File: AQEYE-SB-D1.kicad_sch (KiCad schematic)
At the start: 72 parts, among them J1 GPIO15, J10 ZH06_PicoBlade, J11 DHT20, J12 AGS02MA, J13 +3.3V, J14 MB_PINS, J15 MB_CONNECTOR, J16 GND, J17 USB_D+, J18 USB_D-, J19 +5V, J2 DHT20_PAD, J20 GND, J21 SGP40-D-R4_CONN, J22 SCD40-D-R2_CONN, J23 STEMMA-QT, J24 WS_TVOC, J3 AGS02MA_PAD, J4 GPIO18, J5 ESP_RXD0, J6 ESP_TXD0, J7 I2C_SDA, J8 I2C_SCL, J9 ZH06_Pin, U1 SCD40-D-R2, U2 SGP40-D-R4, U3 AP22804AW5, U4 AP22804AW5

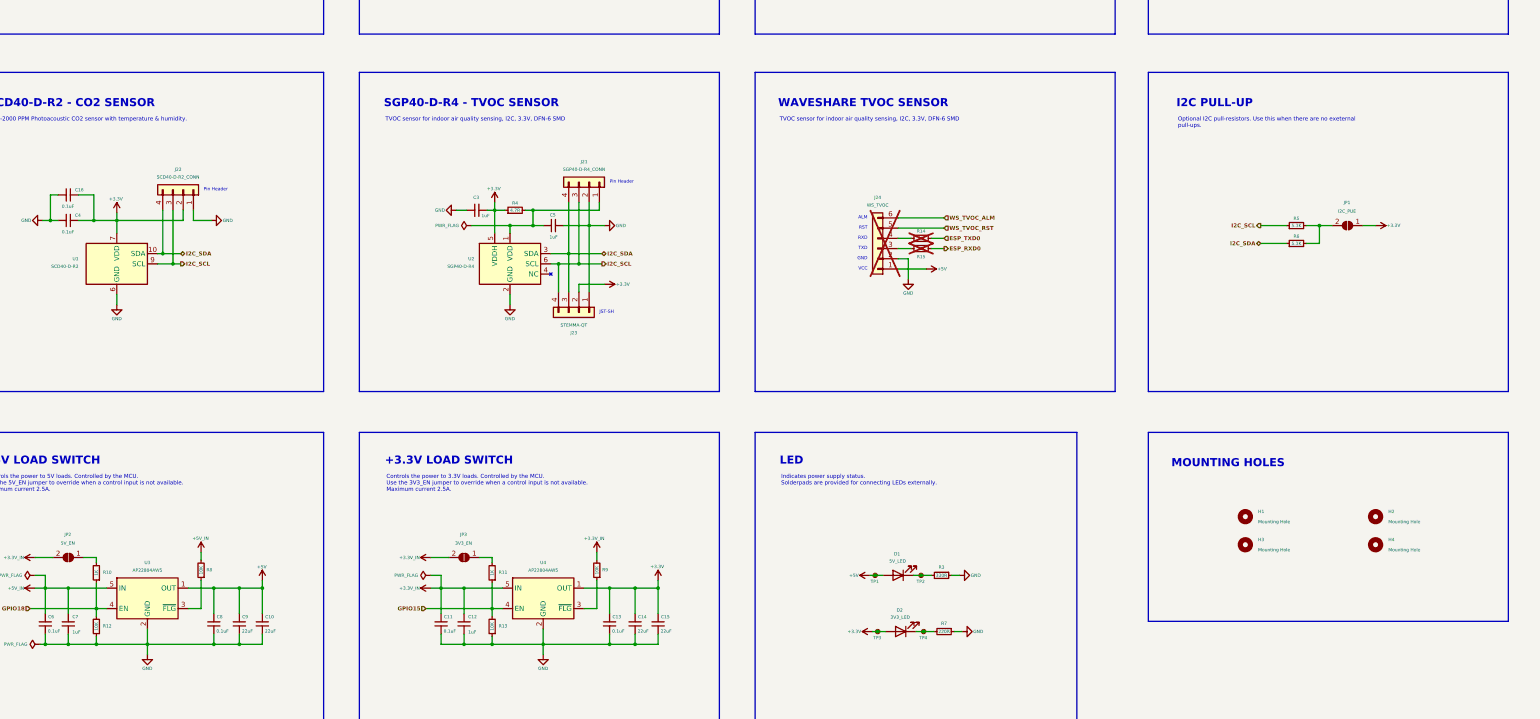
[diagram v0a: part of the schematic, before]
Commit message: Generated manufacturing files
- Schematic
  - Updated BoM.
  - Assigned all MPNs.
  - Added `Group by MPN-DNP` preset.
- PCB
  - Imported all changes to the PCB.
  - Cleaned up the Fab layers.
  - Added CIRCUITSTATE logo and GitHub link to schematic.
  - Applied teardrops.
  - Added board stackup table and characteristics.
  - DRC passes.
- Added KiExport configuration.
- Added Git scripts.
- Generated manufacturing files.
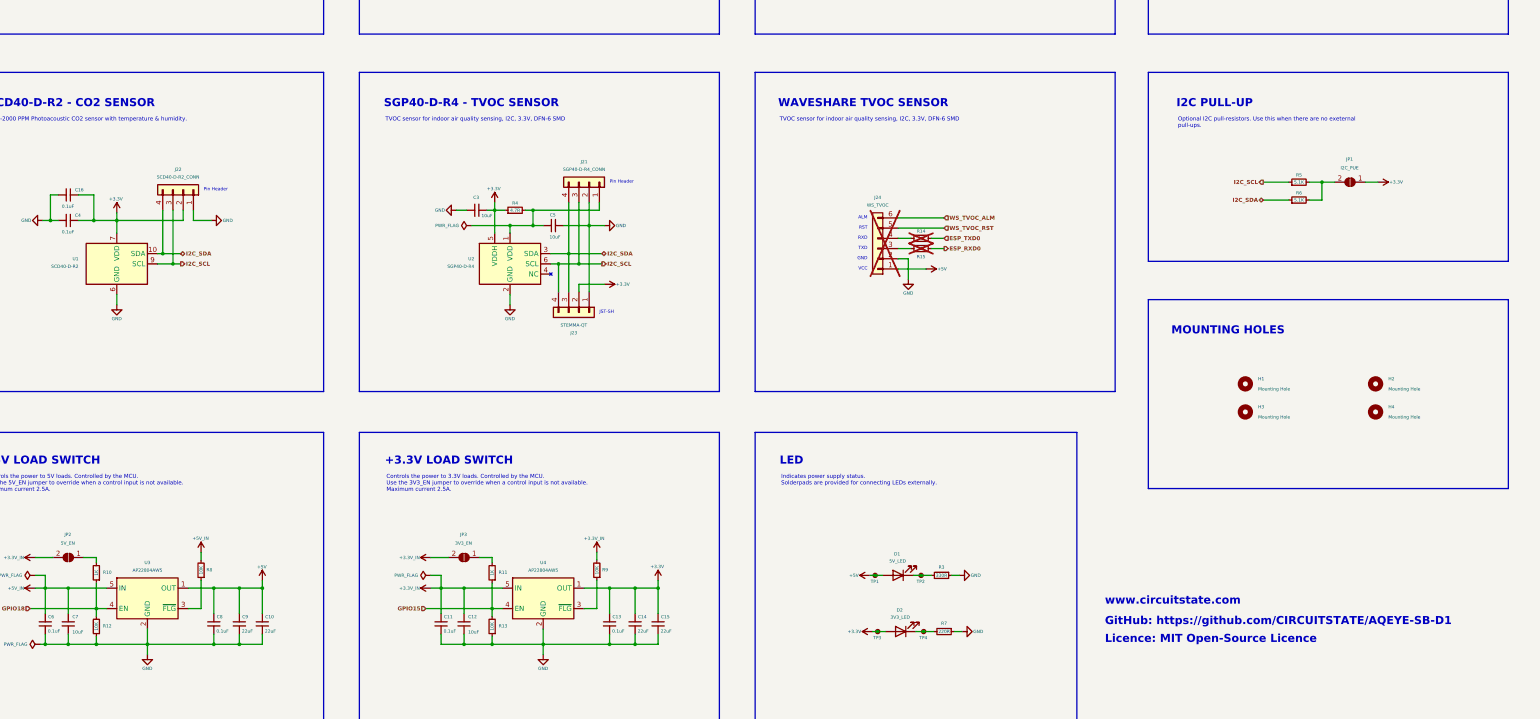
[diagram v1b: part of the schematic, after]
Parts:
- C12, C3, C5, C7: value 1uF -> 10uF; Alt MPN (none) -> CL05A106MP5NUNC, GRM155R61A106ME44D, CGA0402X5R106M100GT, 0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; MFR (none) -> Murata; MPN (none) -> GRM155R61A106ME11D
- D1: Alt MPN (none) -> 19-21SURC/S530-A2/TR8; MFR Everlight -> XINGLIGHT; MPN 19-21SURC/S530-A2/TR8 -> XL-1608SURC-06
- D2: MFR Everlight -> XINGLIGHT; MPN 19-21SURC/S530-A2/TR8 -> XL-1608UOC-06
- J1, J13, J14, J16, J17, J18, J19, J2, J20, J21, J22, J3, J4, J5, J6, J7, J8, J9: MFR (none) -> DNP
- J24: MFR (none) -> DNP; MPN (none) -> DNP; Name (none) -> WS_TVOC
- R1, R10, R11, R14, R15, R2: MFR (none) -> Yageo; MPN (none) -> RC0402FR-071KL
- R12, R13, R8, R9: MFR (none) -> Yageo; MPN (none) -> RC0402FR-0710KL
- R3: MPN RC0402FR-7D220RL -> RC0402FR-07330RL
- R4: MFR (none) -> Yageo; MPN (none) -> RC0402FR-074R7L
- R5, R6: MFR (none) -> Yageo; MPN (none) -> RC0402FR-075K1L
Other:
- note added: "GitHub: https://github.com/CIRCUITSTATE/AQEYE-SB-D1"
- note added: "Licence: MIT Open-Source Licence"
- note added: "www.circuitstate.com"
- moved on the sheet: H1, H2, H3, H4, JP1, R5, R6

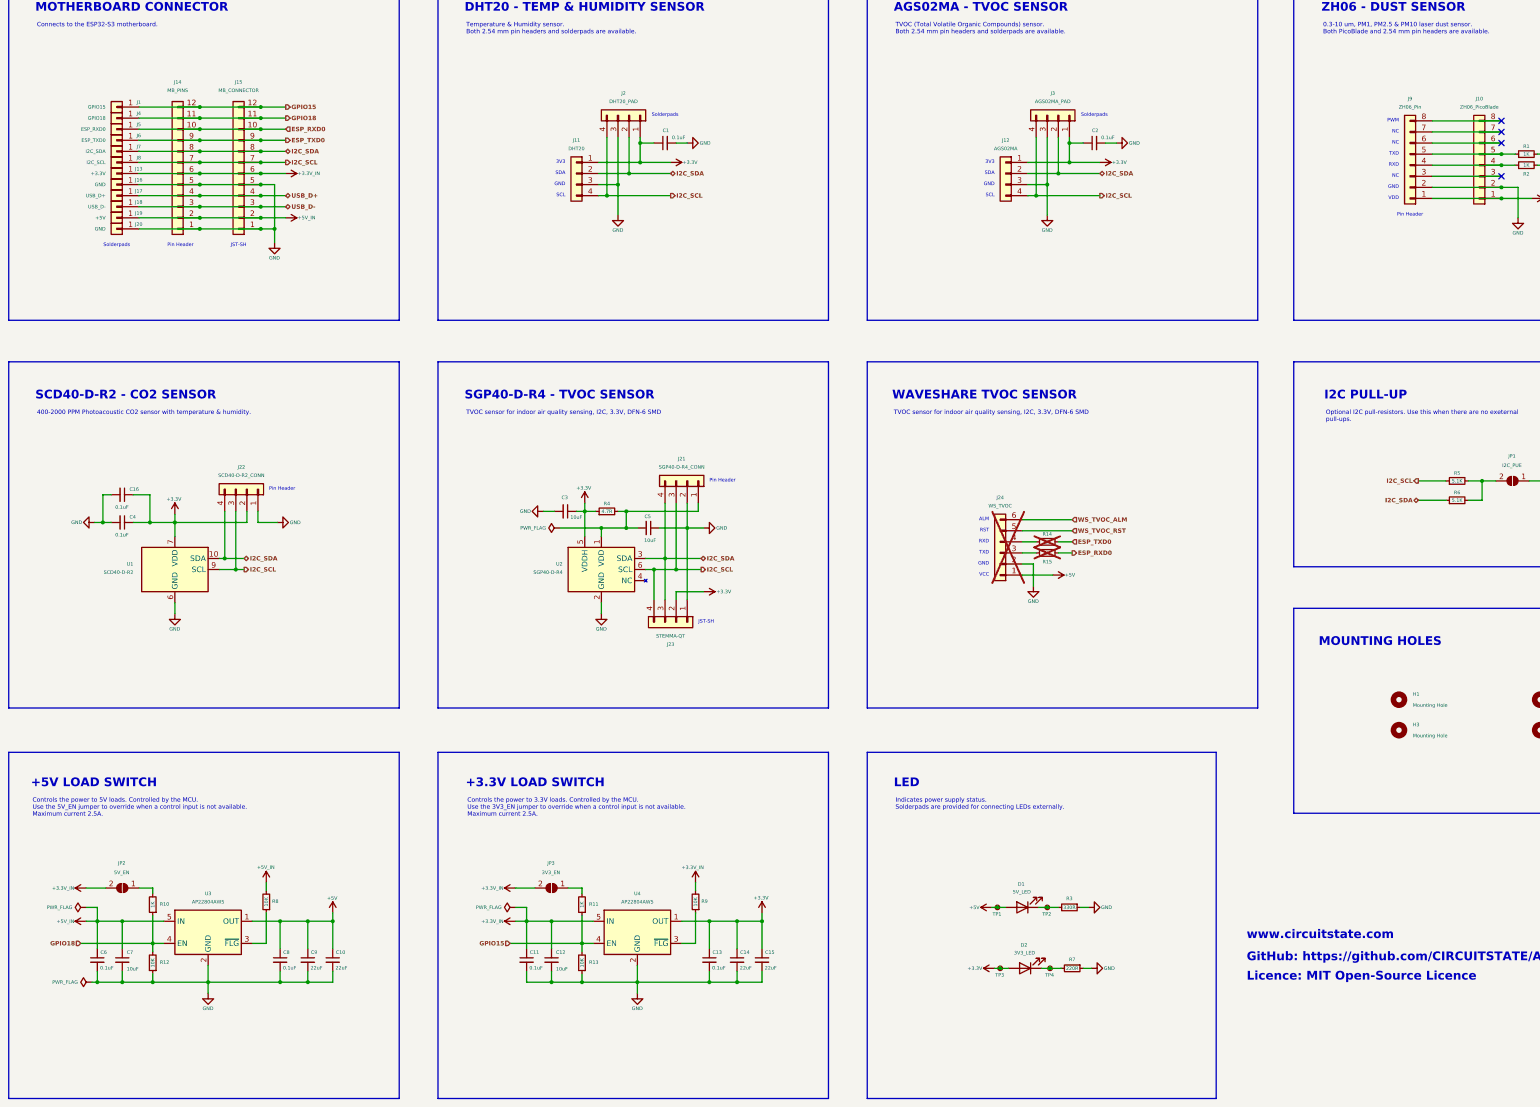
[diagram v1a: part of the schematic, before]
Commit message: Added 5V boost converter
- Schematic
  - Realized that the main board can not supply 5V when the USB is not connected.
  - Added a `TPS61023` 5V boost converter to generate 5V from the 3.3V input.
  - Removed the 5V load switch since the 5V output can not be controlled via the boost converter.
  - The 5V converter enabled by default with a GPIO control.
  - Added `LM66100DCKR` single-channel ideal diode to connect the VBUS to the 5V rail.
  - Reset the annotations.
  - Updated the BoM.
- PCB
  - Imported all changes to the PCB.
  - Placement and routing completed.
  - DRC passes.
  - Updated Fab layers.
  - Updated KiExport configuration.
    - New STEP and VRML options are added.
- Generated manufacturing files.
- No version change.
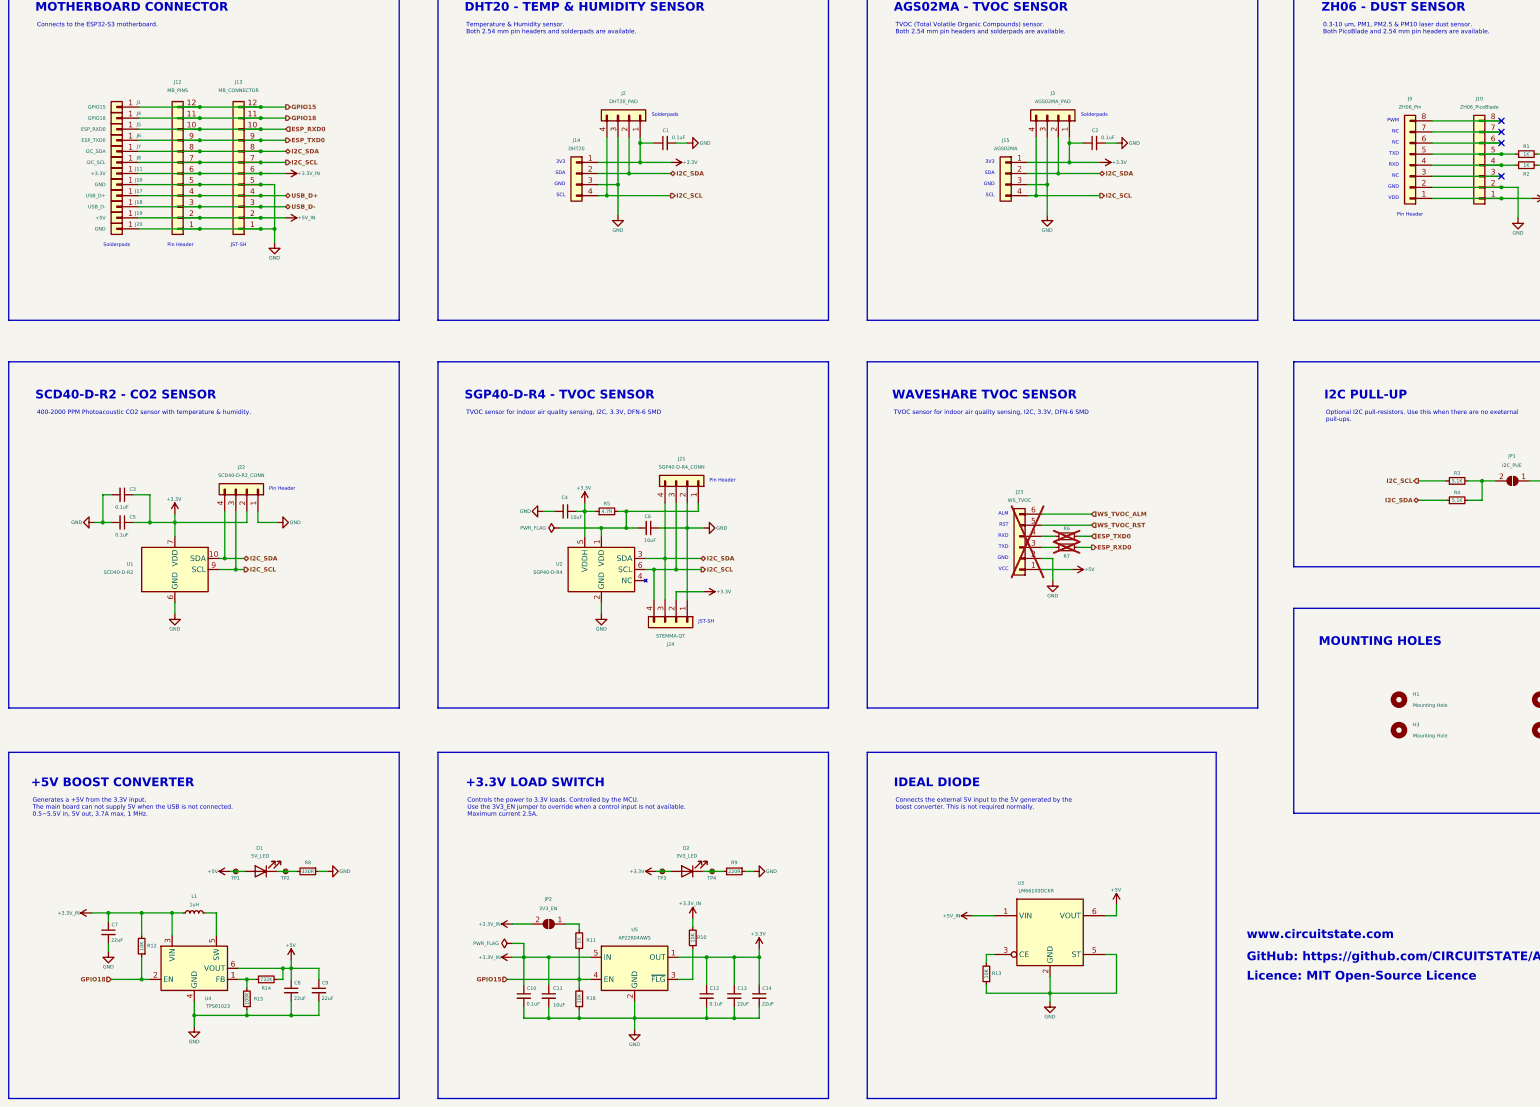
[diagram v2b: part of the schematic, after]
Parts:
- removed C10: 22uF, Capacitor_SMD:C_0603_1608Metric, symbol Device:C_Small
- removed C6: 0.1uF, Capacitor_SMD:C_0402_1005Metric, symbol Device:C_Small
- removed J24: WS_TVOC, symbol Connector_Generic:Conn_01x06
- removed JP2: 5V_EN, CSE_Solder-Jumper:Solder-Jumper-1x2_P1.3mm_Open_Rounded_1.0x1.2mm, symbol Jumper:SolderJumper_2_Open
- removed R10: 1K, Resistor_SMD:R_0402_1005Metric, symbol Device:R_Small
- removed R8: 10K, Resistor_SMD:R_0402_1005Metric, symbol Device:R_Small
- removed U3: AP22804AW5, Package_TO_SOT_SMD:SOT-23-5, symbol Power_Management:AP22804AW5
- added J23: WS_TVOC, symbol Connector_Generic:Conn_01x06
- added L1: 1uH, Inductor_SMD:L_Changjiang_FNR6020S, symbol Device:L_Small
- added R13: 10K, Resistor_SMD:R_0402_1005Metric, symbol Device:R_Small
- added R6, R7: 1K, Resistor_SMD:R_0402_1005Metric, symbol Device:R_Small
- added U3: LM66100DCKR, Package_TO_SOT_SMD:SOT-363_SC-70-6, symbol CSE_Power_Management:LM66100
- added U4: TPS61023, Package_TO_SOT_SMD:SOT-563, symbol CSE_Regulators_Switching:TPS61023
- C7: value 10uF -> 22uF; footprint Capacitor_SMD:C_0402_1005Metric -> Capacitor_SMD:C_0603_1608Metric; Alt MPN CL05A106MP5NUNC, GRM155R61A106ME44D, CGA0402X5R106M100GT, 0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 -> (none); MFR Murata -> Samsung; MPN GRM155R61A106ME11D -> CL10A226MP8NUNE
- C8: value 0.1uF -> 22uF; footprint Capacitor_SMD:C_0402_1005Metric -> Capacitor_SMD:C_0603_1608Metric; MFR Yageo -> Samsung; MPN CC0402KRX5R6BB104 -> CL10A226MP8NUNE
- R14: value 1K -> 732K; MPN RC0402FR-071KL -> RC0402FR-07732KL; now fitted
- R15: value 1K -> 100K; MPN RC0402FR-071KL -> RC0402FR-07100KL; now fitted
- renumbered C11 to C10, C12 to C11, C13 to C12, C14 to C13, C15 to C14, C16 to C3, C3 to C4, C4 to C5, C5 to C6, J13 to J11, J14 to J12, J15 to J13, J11 to J14, J12 to J15, J23 to J24, JP3 to JP2, R9 to R10, R13 to R16, R5 to R3, R6 to R4, R4 to R5, R3 to R8, R7 to R9, U4 to U5
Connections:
- net +3.3V_IN: now also C7.1, R12.2, L1.1, U4.3 (VIN)
- net +5V: now also R14.2, J23.1 (Pin_1), U3.6 (VOUT), U4.6 (VOUT)
- net +5V_IN: now also U3.1 (VIN); no longer C7.1
- net ESP_RXD0: now also R7.2; no longer R15.2
- net ESP_TXD0: now also R6.2; no longer R14.2
- net GND: now also R15.1, J23.2 (Pin_2), R13.1, U3.2 (GND), U3.4 (NC), U3.5 (ST), U4.4 (GND); no longer R12.1
- net GPIO18: now also R12.1, U4.2 (EN); no longer R12.2
- net WS_TVOC_ALM: now also J23.6 (Pin_6)
- net WS_TVOC_RST: now also J23.5 (Pin_5)
- net at R14.1: now also R15.2, U4.1 (FB)
- new net: R13.2, U3.3 (CE)
- new net: L1.2, U4.5 (SW)
- new net: J23.3 (Pin_3), R7.1
- new net: J23.4 (Pin_4), R6.1
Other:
- note added: "+5V BOOST CONVERTER"
- note added: "IDEAL DIODE"
- note removed: "+5V LOAD SWITCH"
- note removed: "LED"
- moved on the sheet: C10, C11, C12, C13, C14, D1, D2, JP2, R10, R11, R16, R8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
